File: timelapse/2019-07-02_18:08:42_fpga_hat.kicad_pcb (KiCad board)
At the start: 4 copper layers, 65 x 56.5 mm, 90 parts, among them J1 2x20, J2 AudioJack3, J3 Conn_02x06_Top_Bottom, J4 Conn_02x06_Top_Bottom, J5 Conn_02x06_Top_Bottom, J6 Conn_01x02, SW1 PTS815, SW2 PTS815, SW3 PTS815, SW4 PTS815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

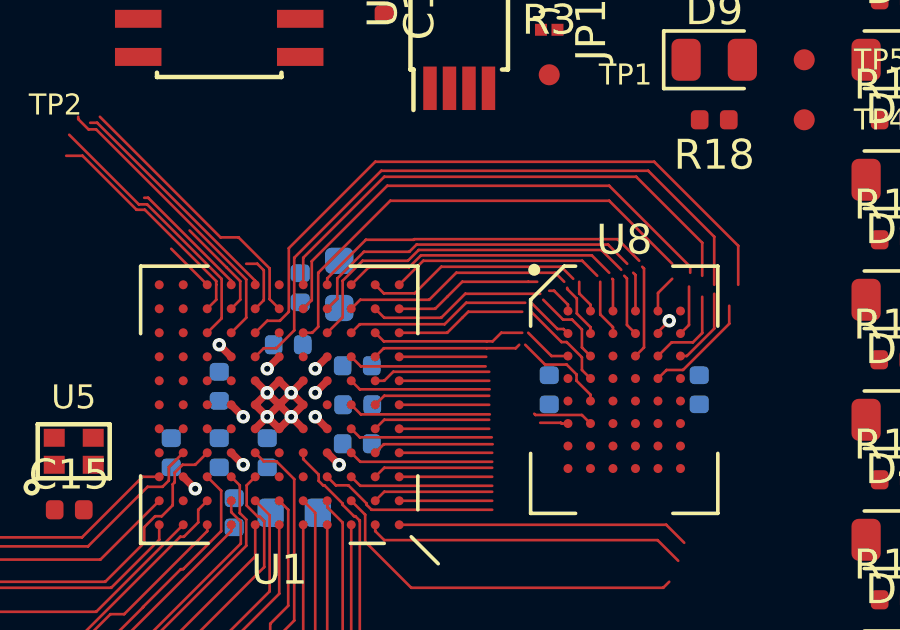
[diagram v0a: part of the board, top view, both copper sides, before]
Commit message: Continue FPGA escape. Start escaping SRAM.
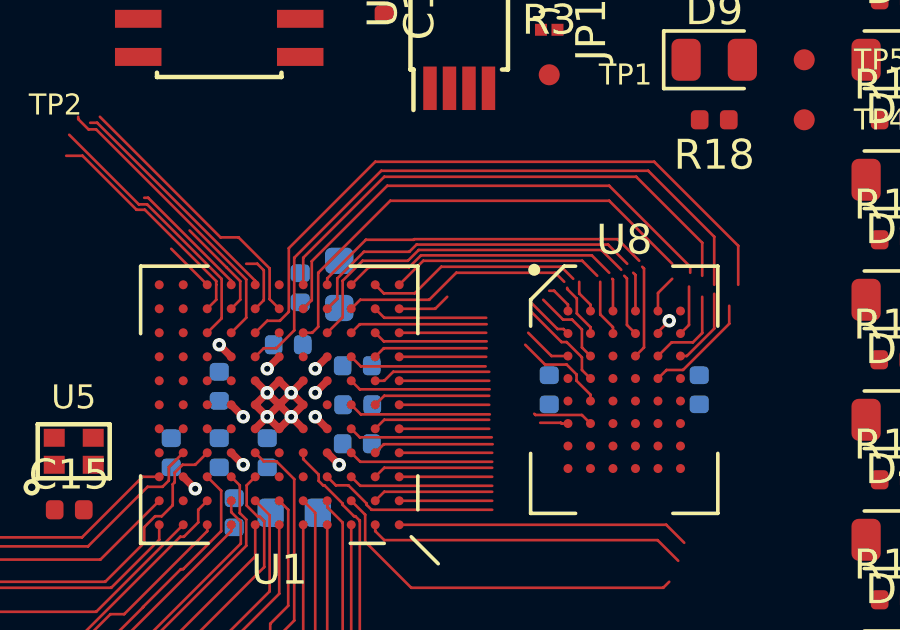
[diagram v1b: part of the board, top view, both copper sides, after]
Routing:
- net /SRAM_A5: track 4.97 -> 1.77 mm
- net /SRAM_A6: track 9.07 -> 6.94 mm
- net /SRAM_A11: track 6.21 -> 4.63 mm
- net /SRAM_A4: track 6.47 -> 4.98 mm
- net /SRAM_A7: track 5.14 -> 3.83 mm
- net /SRAM_A3: track 6.87 -> 5.73 mm
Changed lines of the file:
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@@
     (thickness 1.6)
     (drawings 20)
-    (tracks 444)
+    (tracks 429)
     (zones 0)
     (modules 90)
@@
   (segment (start 144.375 104.125) (end 144.089999 103.839999) (width 0.09) (layer F.Cu) (net 102))
   (segment (start 144.089999 102.289999) (end 144 102.2) (width 0.09) (layer F.Cu) (net 102))
-  (segment (start 136.5 104.1) (end 138.1 104.1) (width 0.09) (layer F.Cu) (net 102))
-  (segment (start 138.1 104.1) (end 138.6 103.6) (width 0.09) (layer F.Cu) (net 102))
-  (segment (start 138.6 103.6) (end 138.8 103.4) (width 0.09) (layer F.Cu) (net 102))
-  (segment (start 138.8 103.4) (end 140.6 103.4) (width 0.09) (layer F.Cu) (net 102))
+  (segment (start 136.5 104.1) (end 139.4 104.1) (width 0.09) (layer F.Cu) (net 102))
   (segment (start 137.7 103.3) (end 138.1 102.9) (width 0.09) (layer F.Cu) (net 103))
   (segment (start 136.5 103.3) (end 137.7 103.3) (width 0.09) (layer F.Cu) (net 103))
-  (segment (start 138.1 102.9) (end 138.6 102.4) (width 0.09) (layer F.Cu) (net 103))
-  (segment (start 138.6 102.4) (end 140.8 102.4) (width 0.09) (layer F.Cu) (net 103))
-  (segment (start 140.8 102.4) (end 141.1 102.4) (width 0.09) (layer F.Cu) (net 103))
   (segment (start 142.6 101.7) (end 143.1 102.2) (width 0.09) (layer F.Cu) (net 104))
   (segment (start 136.5 102.5) (end 137.3 101.7) (width 0.09) (layer F.Cu) (net 104))
@@
   (segment (start 135.985001 104.614999) (end 139.414999 104.614999) (width 0.09) (layer F.Cu) (net 111))
   (segment (start 135.7 104.9) (end 135.985001 104.614999) (width 0.09) (layer F.Cu) (net 111))
-  (segment (start 139.414999 104.614999) (end 140.385001 104.614999) (width 0.09) (layer F.Cu) (net 111))
-  (segment (start 140.385001 104.614999) (end 140.5 104.5) (width 0.09) (layer F.Cu) (net 111))
   (segment (start 135.985001 104.385001) (end 139.414999 104.385001) (width 0.09) (layer F.Cu) (net 112))
   (segment (start 135.7 104.1) (end 135.985001 104.385001) (width 0.09) (layer F.Cu) (net 112))
-  (segment (start 139.414999 104.385001) (end 139.614999 104.385001) (width 0.09) (layer F.Cu) (net 112))
-  (segment (start 139.614999 104.385001) (end 139.9 104.1) (width 0.09) (layer F.Cu) (net 112))
-  (segment (start 139.9 104.1) (end 140.6 104.1) (width 0.09) (layer F.Cu) (net 112))
   (segment (start 144.660001 104.589999) (end 144.660001 101.960001) (width 0.09) (layer F.Cu) (net 113))
   (segment (start 144.375 104.875) (end 144.660001 104.589999) (width 0.09) (layer F.Cu) (net 113))
   (segment (start 144.660001 101.960001) (end 144.6 101.9) (width 0.09) (layer F.Cu) (net 113))
-  (segment (start 137.9 103.6) (end 138.7 102.8) (width 0.09) (layer F.Cu) (net 113))
+  (segment (start 136 103.6) (end 139.4 103.6) (width 0.09) (layer F.Cu) (net 113))
   (segment (start 135.7 103.3) (end 136 103.6) (width 0.09) (layer F.Cu) (net 113))
-  (segment (start 136 103.6) (end 137.9 103.6) (width 0.09) (layer F.Cu) (net 113))
-  (segment (start 138.7 102.8) (end 141.2 102.8) (width 0.09) (layer F.Cu) (net 113))
   (segment (start 137.014999 102.785001) (end 137.9 101.9) (width 0.09) (layer F.Cu) (net 114))
   (segment (start 141.9 101.9) (end 142.3 102.3) (width 0.09) (layer F.Cu) (net 114))
@@
   (segment (start 135.219989 105.219989) (end 139.380011 105.219989) (width 0.09) (layer F.Cu) (net 120))
   (segment (start 134.9 104.9) (end 135.219989 105.219989) (width 0.09) (layer F.Cu) (net 120))
-  (segment (start 138.014999 103.814999) (end 138.729998 103.1) (width 0.09) (layer F.Cu) (net 121))
-  (segment (start 138.729998 103.1) (end 140.7 103.1) (width 0.09) (layer F.Cu) (net 121))
+  (segment (start 135.185001 103.814999) (end 139.414999 103.814999) (width 0.09) (layer F.Cu) (net 121))
   (segment (start 134.9 104.1) (end 135.185001 103.814999) (width 0.09) (layer F.Cu) (net 121))
-  (segment (start 135.185001 103.814999) (end 138.014999 103.814999) (width 0.09) (layer F.Cu) (net 121))
   (segment (start 137.5 103) (end 138.4 102.1) (width 0.09) (layer F.Cu) (net 122))
   (segment (start 134.9 103.3) (end 135.2 103) (width 0.09) (layer F.Cu) (net 122))
